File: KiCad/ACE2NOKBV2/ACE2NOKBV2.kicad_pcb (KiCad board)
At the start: 2 copper layers, 160 x 100 mm, 105 parts, among them IC1 78T, IC2 74367N, Q1 2N3904, Q2 2N3904, Q3 BC237, X1 6.556MHz

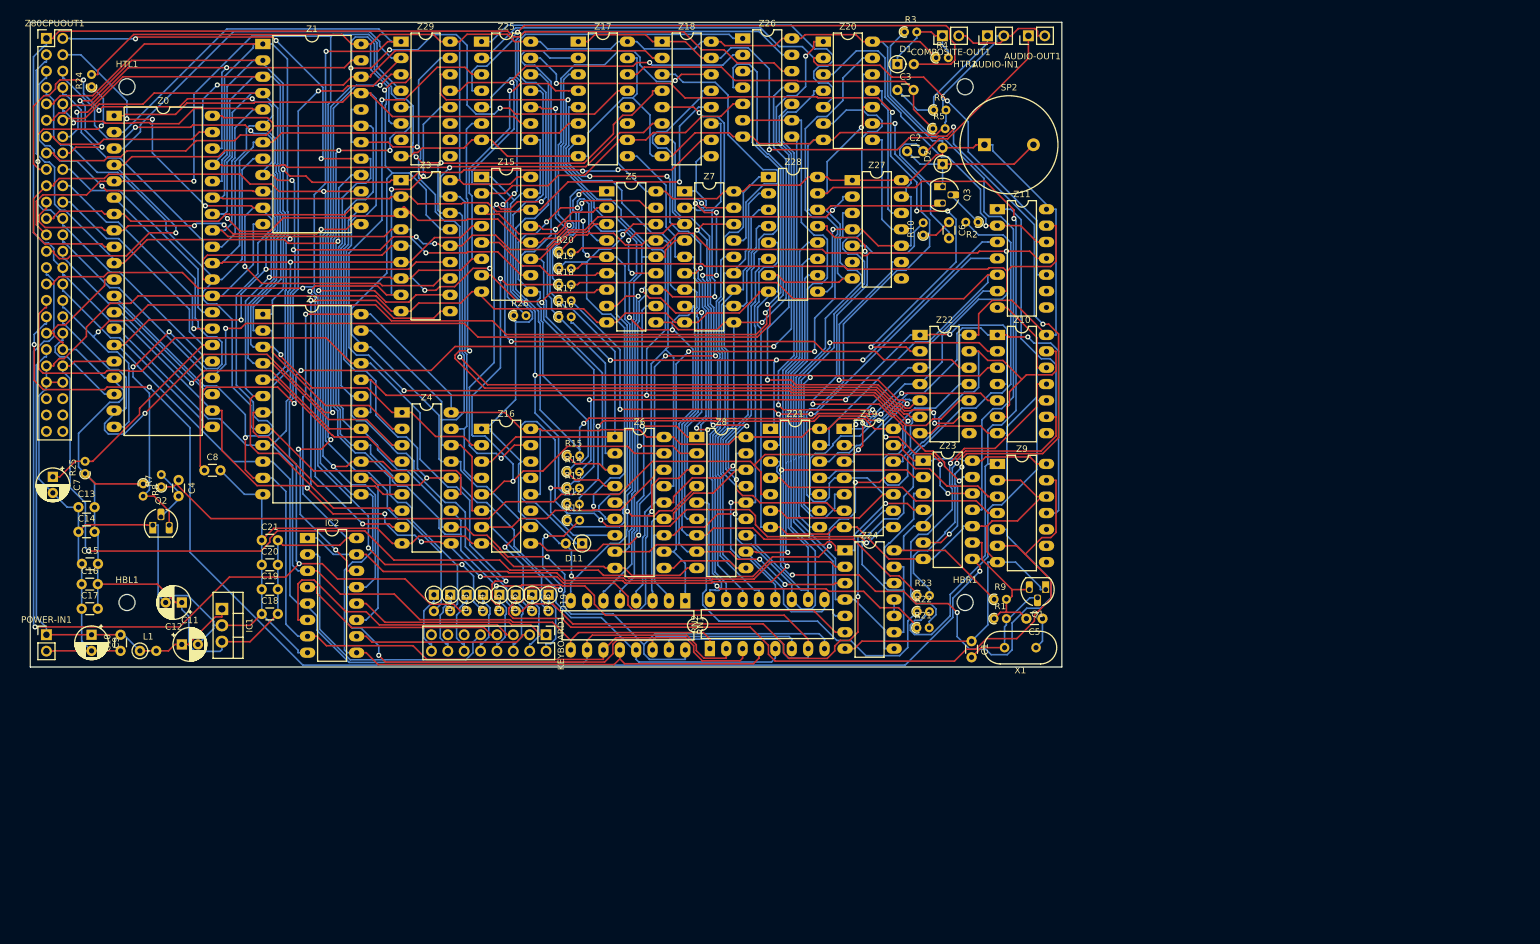
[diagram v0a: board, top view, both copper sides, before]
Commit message: Correct all routing.
Signed-off-by: John Bradley <flypie@rocketmail.com>
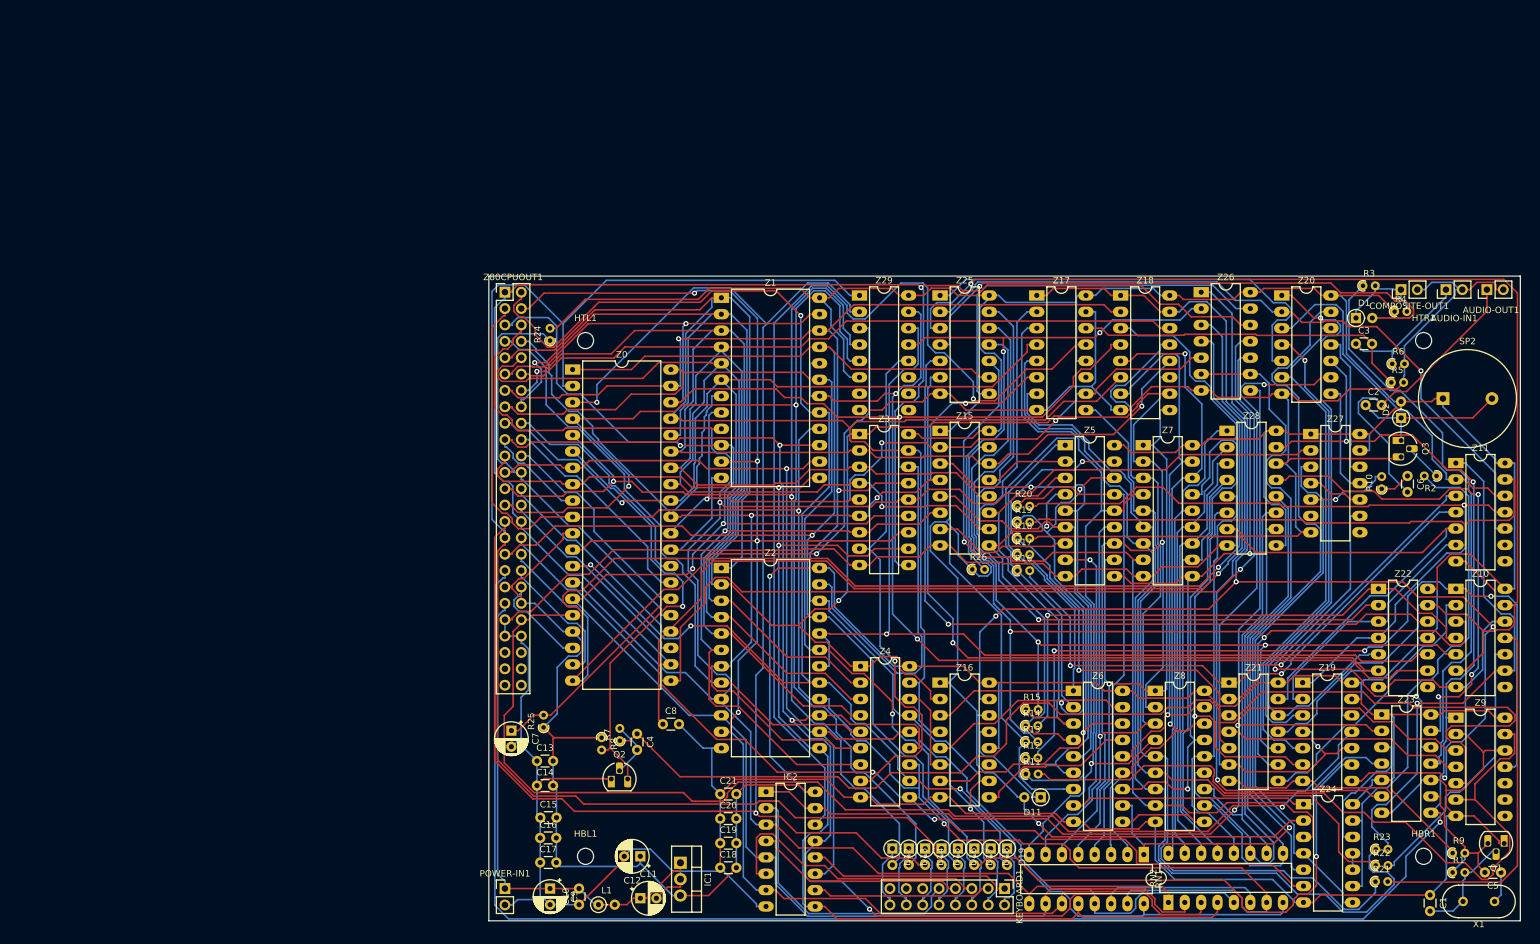
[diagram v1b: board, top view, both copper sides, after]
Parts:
- moved Z19 81.3 mm to (197.4, 102.4)
- moved AUDIO-IN1 81.3 mm to (219.6, 41.5)
- moved AUDIO-OUT1 81.3 mm to (225.9, 41.5)
- moved C1 81.3 mm to (217.1, 135.4)
- moved C10 81.3 mm to (85.1, 136.9)
- moved C11 81.3 mm to (94.6, 135.9)
- moved C12 81.3 mm to (94.6, 129.4)
- moved C13 81.3 mm to (78.6, 114.6)
- moved C14 81.3 mm to (78.6, 118.4)
- moved C15 81.3 mm to (79.1, 123.4)
- moved C17 81.3 mm to (79.1, 130.3)
- moved C19 81.3 mm to (107.0, 127.3)
- moved C2 81.3 mm to (207.1, 59.4)
- moved C3 81.3 mm to (205.6, 49.9)
- moved C4 81.3 mm to (94.1, 110.4)
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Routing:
- net /CNT3: track 148.8 -> 113.6 mm, vias 2 -> 0
- net Net-(Z2-Pad18): track 187.5 -> 155.6 mm, vias 2 -> 1
- net Net-(Z17-Pad1): track 165.7 -> 134.2 mm, vias 5 -> 1
- net /A13: track 277.8 -> 248.9 mm, vias 3 -> 2
- net Net-(R20-Pad1): track 107.9 -> 83.3 mm, vias 1 -> 0
- net /A0: track 238.1 -> 214.0 mm, vias 2 -> 3
- net Net-(R23-Pad1): track 123.8 -> 147.5 mm
- net Net-(D11-Pad2): track 202.5 -> 225.5 mm
- net /CNT8: track 231.6 -> 210.1 mm, vias 3 -> 1
- net /A1: track 214.8 -> 193.8 mm, vias 1 -> 3
- net Net-(R22-Pad1): track 139.8 -> 119.2 mm, vias 3 -> 0
- net /A11: track 234.0 -> 214.4 mm
- net /A3: track 215.0 -> 233.7 mm, vias 3 -> 1
- net /CNT2: track 89.0 -> 71.1 mm, vias 2 -> 0
- net /A2: track 243.1 -> 225.7 mm, vias 5 -> 2
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
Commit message: Tidy add Zilog Logo.
Signed-off-by: John Bradley <flypie@rocketmail.com>
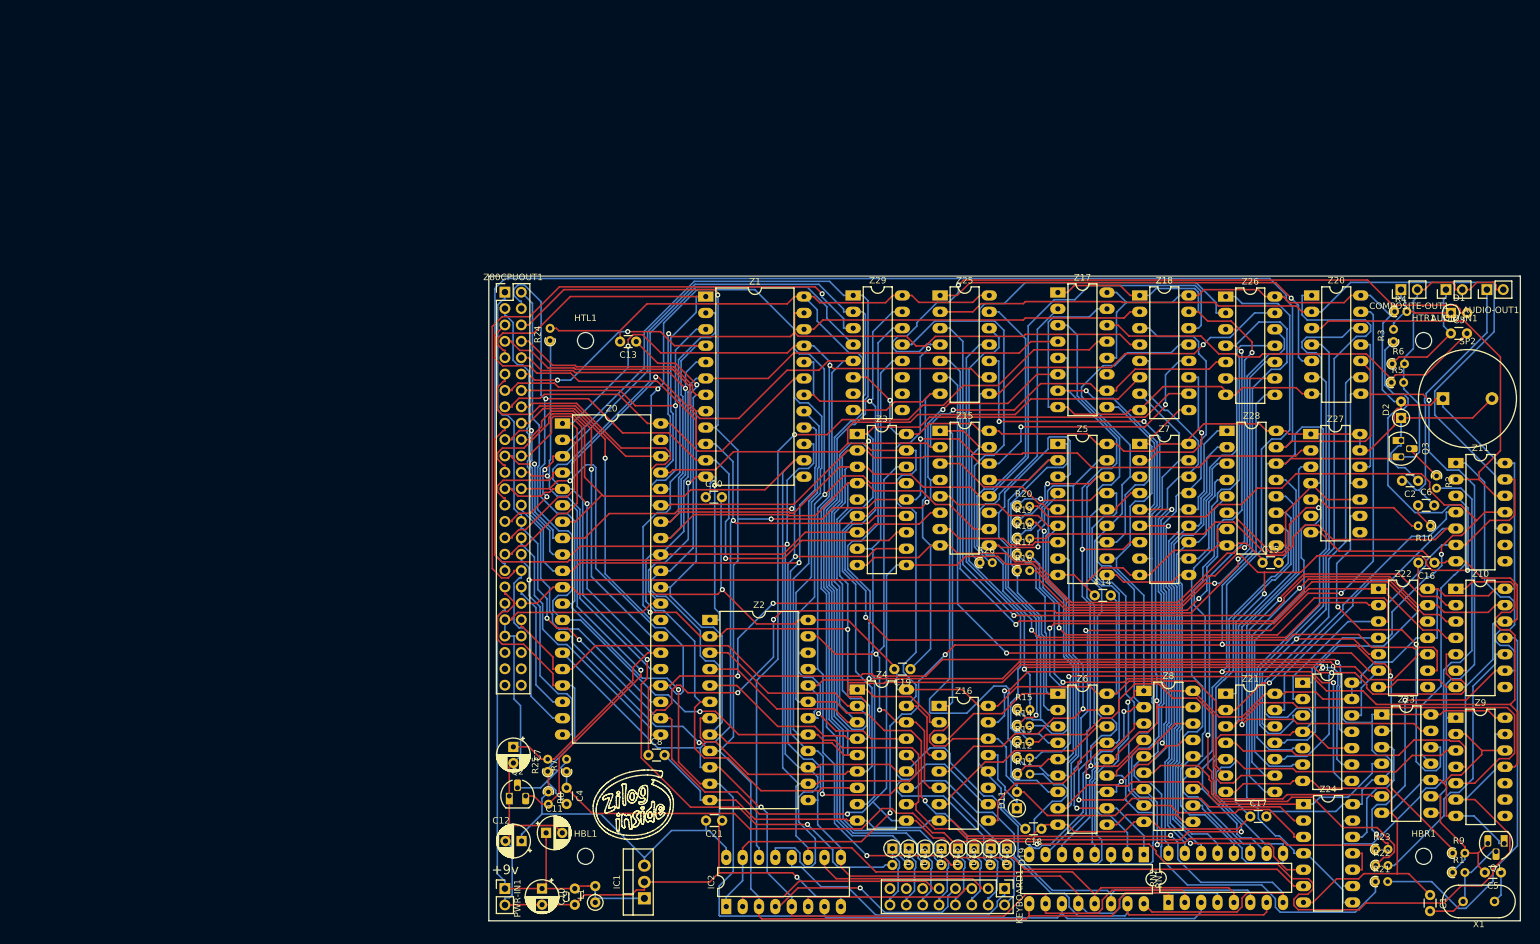
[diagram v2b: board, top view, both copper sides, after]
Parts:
- moved C16 145.1 mm to (217.8, 83.8), turned to 180 degrees
- moved C15 118.8 mm to (191.1, 83.8)
- moved C17 110.4 mm to (189.2, 123.2)
- moved C14 91.4 mm to (165.1, 88.9)
- moved C13 66.9 mm to (94.0, 49.5), turned to 180 degrees
- moved C18 50.2 mm to (156.8, 125.1), turned to 180 degrees
- moved C20 49.9 mm to (104.8, 73.7)
- moved C19 40.0 mm to (136.5, 100.3), turned to 180 degrees
- moved IC2 18.8 mm to (108.0, 137.2), turned to 90 degrees
- moved C12 18.6 mm to (76.2, 127.0)
- moved C11 17.8 mm to (80.0, 125.7)
- moved Q2 16.0 mm to (74.3, 120.0)
- moved C3 14.8 mm to (220.3, 48.3)
- moved D1 14.7 mm to (220.3, 45.1)
- moved C2 14.3 mm to (215.3, 71.1), turned to 180 degrees
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- renumbered POWER-IN1 to PWR-IN1
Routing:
- net GND: track 760.6 -> 839.2 mm, vias 0 -> 3
- net /A13: track 248.9 -> 180.4 mm
- net /A9: track 224.8 -> 270.9 mm
- net //VHOLD: track 189.8 -> 148.6 mm, vias 4 -> 3
- net /A0: track 214.0 -> 254.6 mm, vias 3 -> 2
- net /A12: track 226.6 -> 189.3 mm
- net /EAR: track 155.4 -> 122.6 mm
- net /DA4: track 204.3 -> 236.7 mm, vias 1 -> 0
- net //INT: track 178.3 -> 149.2 mm
- net /CNT8: track 210.1 -> 181.4 mm
- net /A10: track 231.1 -> 257.5 mm
- net Net-(RN1-Pad7): track 139.2 -> 112.7 mm
- net /A1: track 193.8 -> 220.2 mm, vias 3 -> 2
- net Net-(RN1-Pad3): track 103.3 -> 128.0 mm, vias 2 -> 0
- net /A2: track 225.7 -> 250.3 mm, vias 2 -> 0
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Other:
- board text added: "+9v"

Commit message: Add Edge board to convert PINs to EDGECONNECTOR.
Signed-off-by: John Bradley <flypie@rocketmail.com>
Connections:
- Z26 pad 11: Net-(Z26-Pad11) -> /#WE
- Z5 pad 10: Net-(Z26-Pad11) -> /#WE
- Z6 pad 10: Net-(Z26-Pad11) -> /#WE
- Z7 pad 10: Net-(Z26-Pad11) -> /#WE
- Z8 pad 10: Net-(Z26-Pad11) -> /#WE
- Z80CPUOUT1 pad 1: //WR -> /#WE
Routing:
- net Net-(Z26-Pad11): track 117.0 -> 0.00 mm
- net /#WE: track 0.00 -> 117.0 mm

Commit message: Improve consitancy.
Signed-off-by: John Bradley <flypie@rocketmail.com>
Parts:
- added R32: 1K0, Resistor_THT:R_Axial_DIN0204_L3.6mm_D1.6mm_P2.54mm_Vertical, F.Cu at (96.5, 41.7)
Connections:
- Z26 pad 11: /#WE -> Net-(R32-Pad2)
- Z5 pad 10: /#WE -> Net-(R32-Pad2)
- Z6 pad 10: /#WE -> Net-(R32-Pad2)
- Z7 pad 10: /#WE -> Net-(R32-Pad2)
- Z8 pad 10: /#WE -> Net-(R32-Pad2)
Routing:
- net Net-(R32-Pad2): track 0.00 -> 222.2 mm, vias 0 -> 2
- net /DA5: track 235.2 -> 377.6 mm, vias 2 -> 3
- net #NMI: track 777.6 -> 907.2 mm, vias 2 -> 13
- net /#WE: track 117.0 -> 23.9 mm
- net GND: track 839.2 -> 928.6 mm, vias 3 -> 9
- net #CPUCLK: track 305.9 -> 229.7 mm, vias 1 -> 2
- net /DA1: track 257.0 -> 330.8 mm, vias 2 -> 5
- net Net-(Z2-Pad18): track 169.2 -> 239.6 mm, vias 1 -> 3
- net /A10: track 257.5 -> 319.8 mm, vias 2 -> 4
- net /DA6: track 232.9 -> 277.7 mm, vias 2 -> 3
- net Net-(Z24-Pad5): track 109.0 -> 151.5 mm
- net /A11: track 203.4 -> 244.3 mm, vias 3 -> 5
- net /A8: track 246.9 -> 285.2 mm, vias 4 -> 8
- net Net-(Z1-Pad18): track 169.7 -> 206.9 mm
- net /A4: track 257.5 -> 220.8 mm, vias 2 -> 5
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
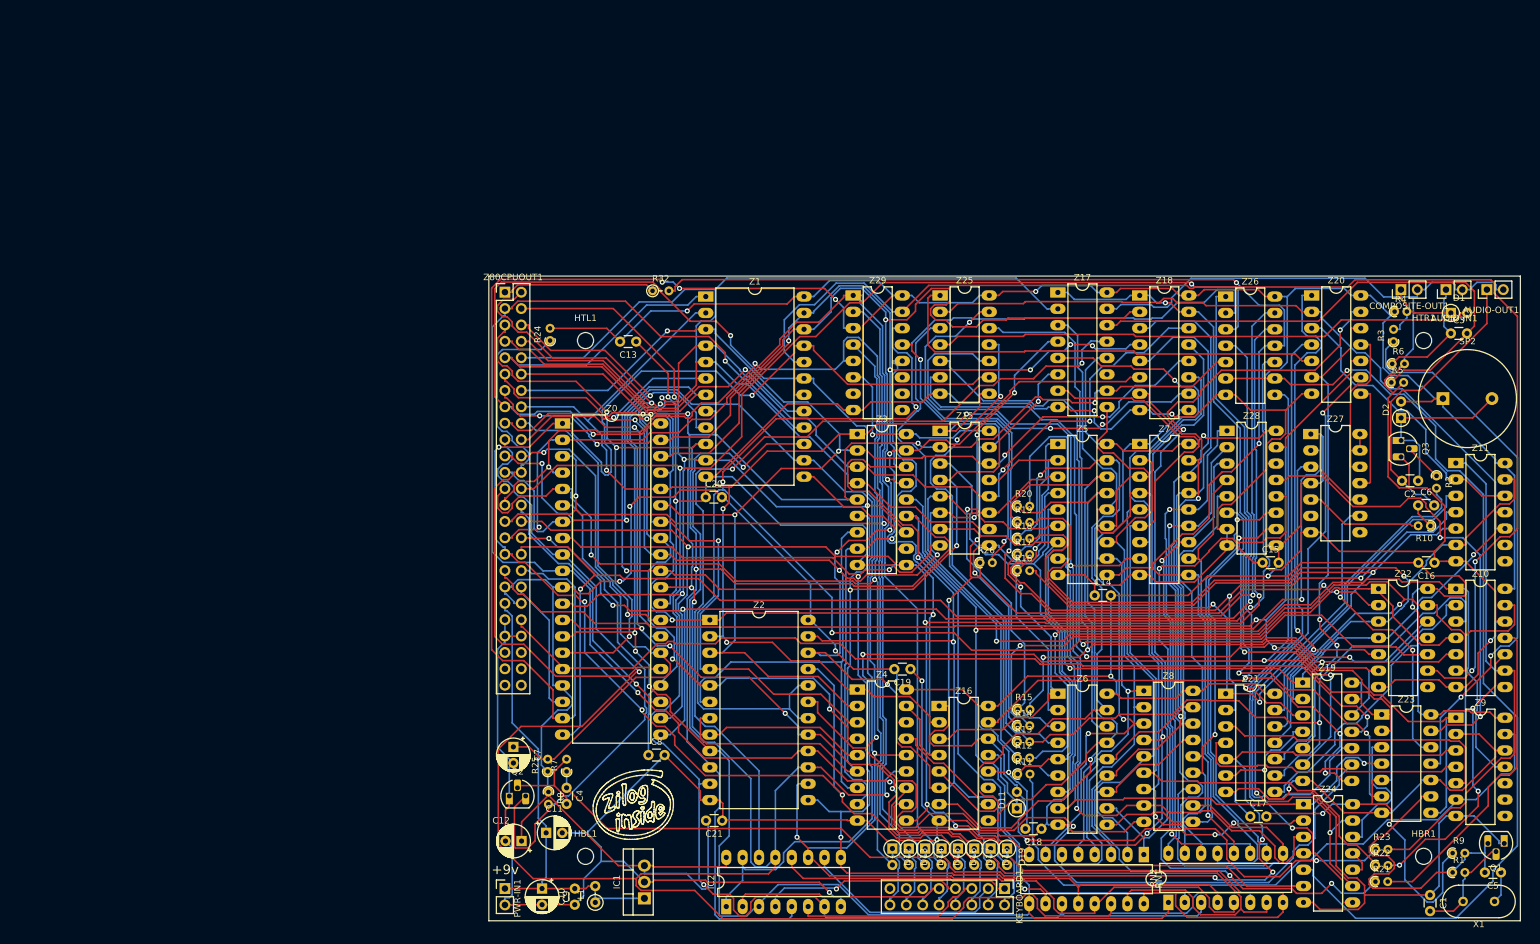
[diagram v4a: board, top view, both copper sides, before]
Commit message: Change capacitor spec, rpve speeak and replace with resistor protected pins.
Signed-off-by: John Bradley <flypie@rocketmail.com>
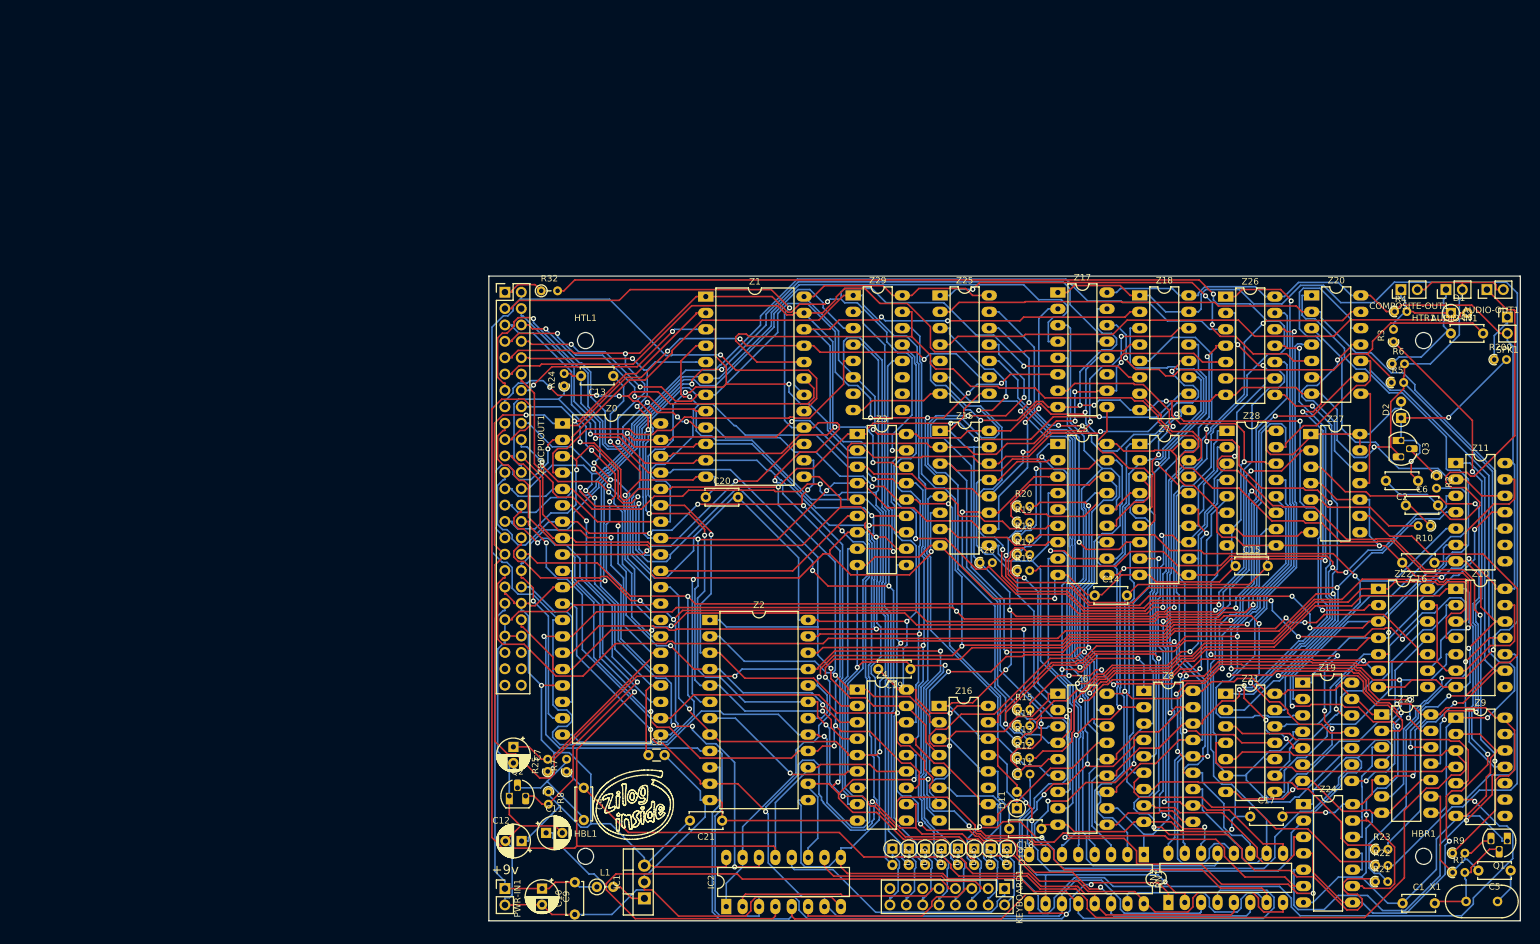
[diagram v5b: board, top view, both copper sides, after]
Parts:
- removed SP2: AL11P, Buzzer_Beeper:Buzzer_15x7.5RM7.6
- added R200: 200, Resistor_THT:R_Axial_DIN0204_L3.6mm_D1.6mm_P1.90mm_Vertical, F.Cu at (227.1, 52.3)
- added SPK1: Conn_01x02, Connector_PinHeader_2.54mm:PinHeader_1x02_P2.54mm_Vertical, F.Cu at (229.1, 45.7)
- C1, C10, C13, C14, C15, C16, C17, C18, C19, C2, C20, C21, C3, C4, C5, C6: footprint Capacitor_THT:C_Disc_D3.0mm_W1.6mm_P2.50mm -> Capacitor_THT:C_Disc_D5.0mm_W2.5mm_P5.00mm
- moved R32 17.3 mm to (79.2, 41.7)
- moved R24 7.35 mm to (82.8, 56.4)
- moved C13 6.41 mm to (90.4, 54.9)
- moved C1 4.46 mm to (212.9, 136.7), turned to 0 degrees
- moved C15 4.22 mm to (186.9, 84.3)
- moved C4 2.67 mm to (85.9, 118.7)
- moved L1 2.43 mm to (87.9, 134.1), turned to 0 degrees
- moved C6 1.90 mm to (213.4, 74.9)
- moved C5 1.53 mm to (229.6, 131.6)
- moved C10 1.52 mm to (84.5, 138.4)
- moved Q1 0.61 mm to (229.1, 127.0)
- moved X1 0.46 mm to (227.6, 136.4)
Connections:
- C11 pad 1: +9V -> +9Vsm
- IC1 pad 1: +9V -> +9Vsm
- L1 pad 2: +9V -> +9Vsm
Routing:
- net Net-(Z2-Pad18): track 239.6 -> 168.5 mm, vias 3 -> 4
- net /A2: track 228.1 -> 296.4 mm, vias 7 -> 4
- net /A10: track 319.8 -> 254.3 mm, vias 4 -> 9
- net //MREQ: track 167.1 -> 105.9 mm, vias 3 -> 1
- net #CPUCLK: track 229.7 -> 287.4 mm
- net Net-(IC2-Pad4): track 31.2 -> 86.6 mm, vias 1 -> 0
- net Net-(Z17-Pad1): track 119.1 -> 172.1 mm, vias 3 -> 2
- net /A3: track 259.4 -> 210.3 mm, vias 3 -> 8
- net /CNT5: track 177.4 -> 226.0 mm
- net /DA5: track 377.6 -> 332.4 mm, vias 3 -> 5
- net Net-(Z23-Pad4): track 99.1 -> 139.9 mm, vias 1 -> 2
- net /EAR: track 138.9 -> 177.4 mm, vias 2 -> 5
- net Net-(R26-Pad2): track 108.1 -> 145.4 mm, vias 2 -> 4
- net Net-(Z24-Pad4): track 84.6 -> 121.4 mm, vias 1 -> 3
- net /CNT3: track 104.1 -> 140.4 mm, vias 0 -> 1
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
